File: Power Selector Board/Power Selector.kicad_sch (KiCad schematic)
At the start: 23 parts, among them J101 MSD-DB01M-12P, J102 MSD-DB01F-12P_1, J103 64900221122, J104 64900221122, J105 64900221122, K101 G6SK-2G DC24, K102 J115F11C24VDCSH.9, K103 J115F11C24VDCSH.9, U101 1720466, U102 LMW78_24-0.3RL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

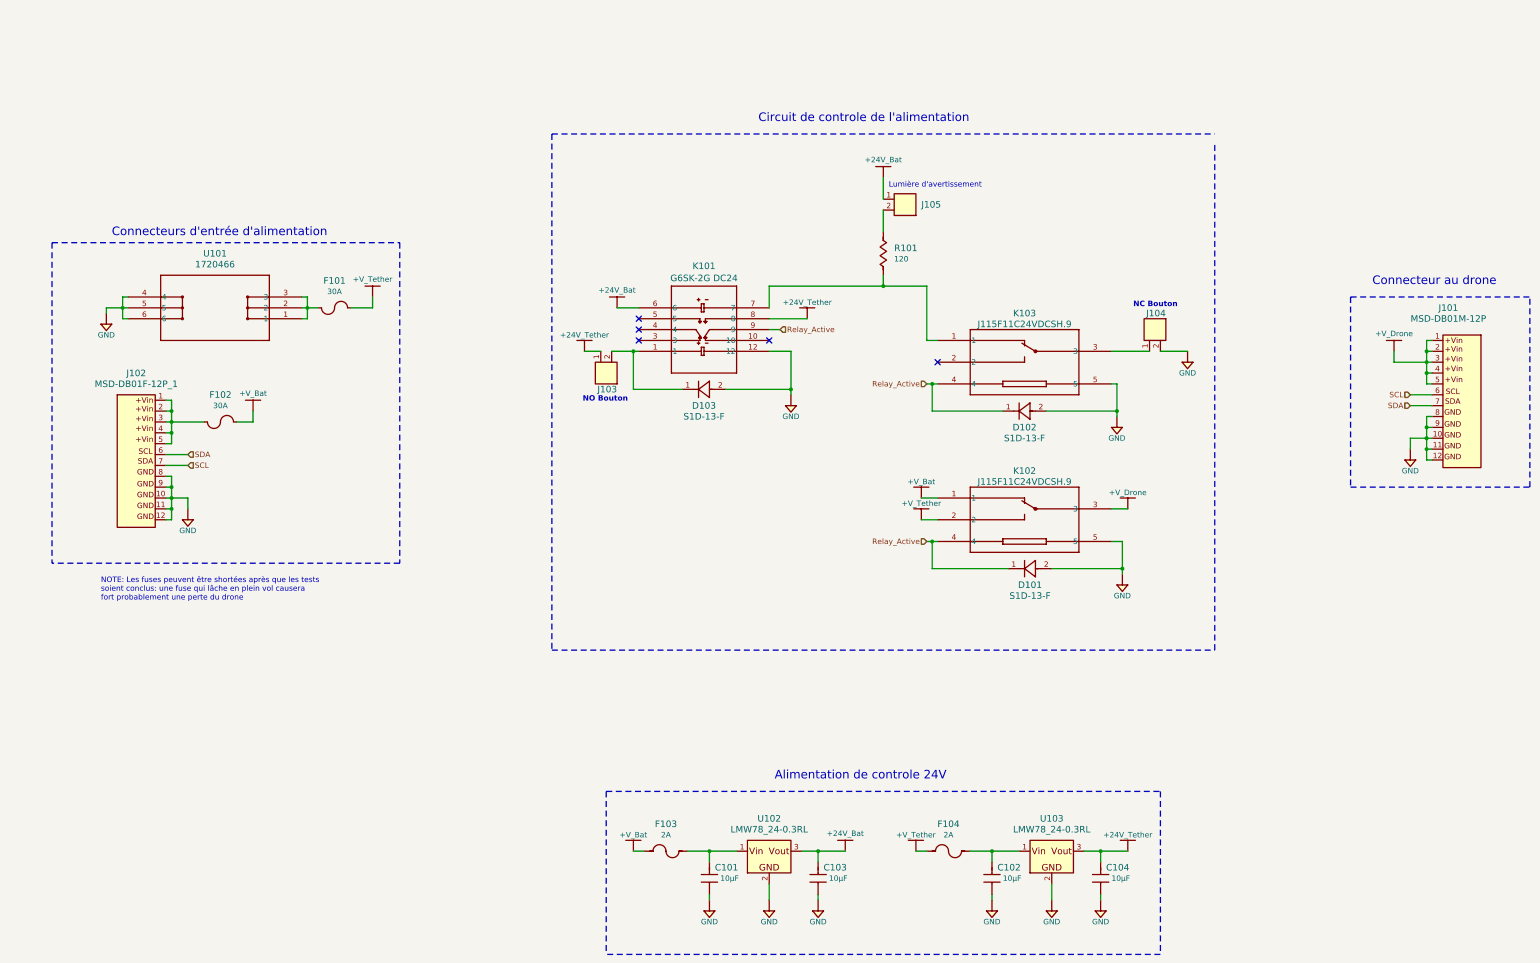
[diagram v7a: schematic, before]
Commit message: Ajout des deux PCB (droit et gauche) sur le meme PCB
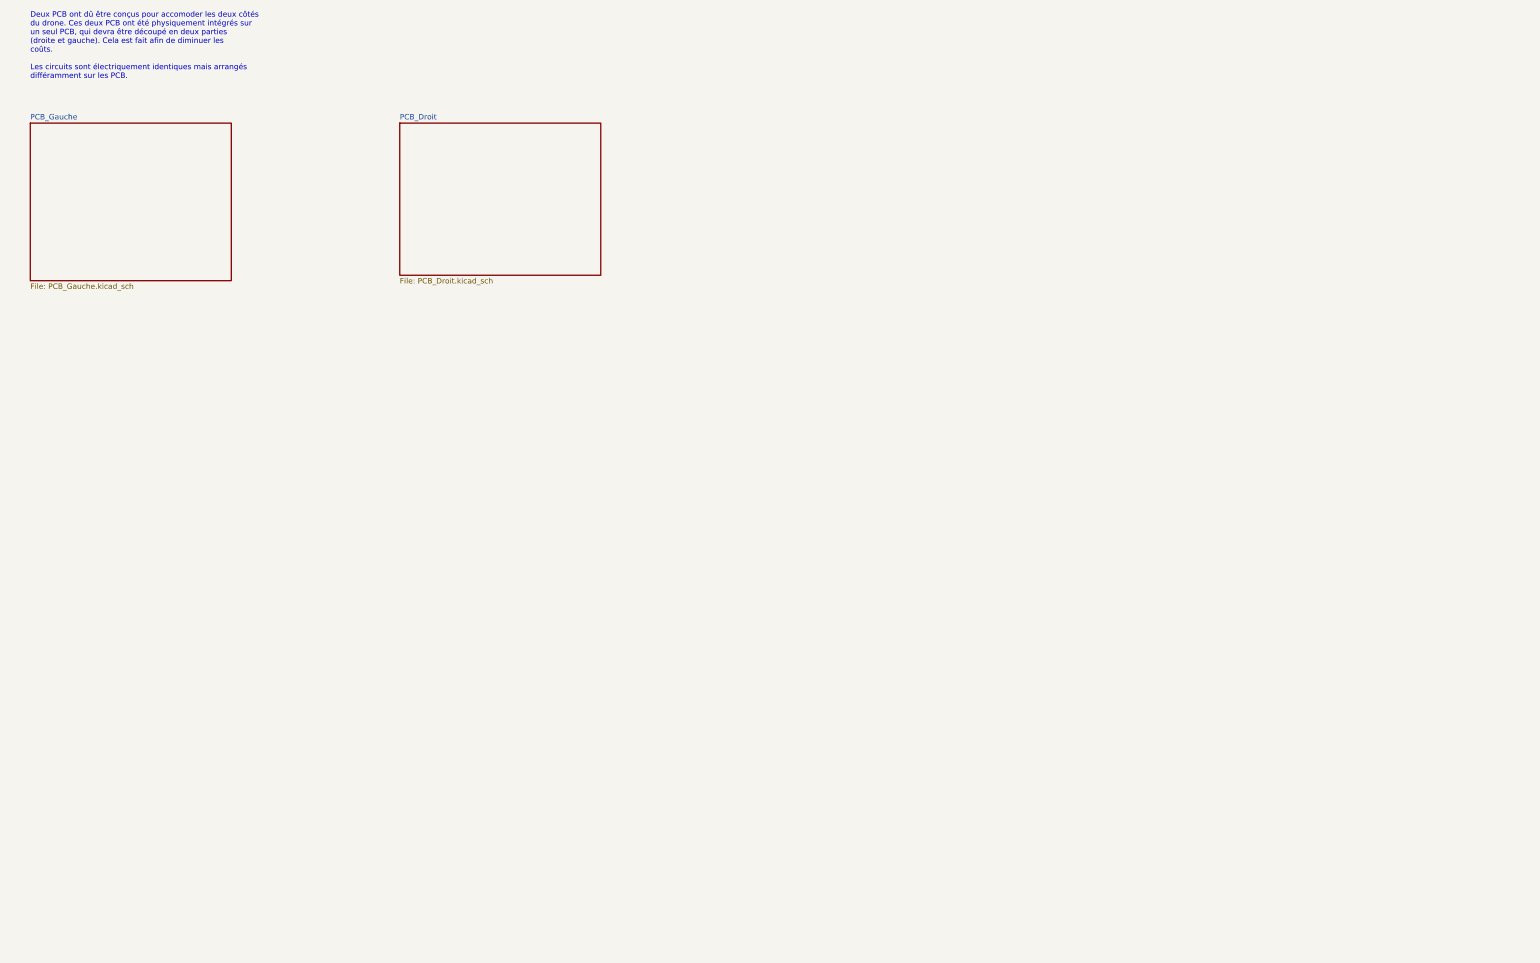
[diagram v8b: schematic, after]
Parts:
- removed C101, C102, C103, C104: GRM32EC72A106ME05L, Capacitors:C1210, symbol Capacitors:GRM32EC72A106ME05L
- removed D101, D102, D103: S1D-13-F, Diodes:SMA_DIO, symbol Diodes:S1D-13-F
- removed F101, F102: 047706.3MRET1P, Fuses:3587TR, symbol Fuses:047706.3MRET1P
- removed F103, F104: 0698Q2000-02, Fuses:TE5_395, symbol Fuses:0698Q2000-02
- removed J101: MSD-DB01M-12P, Connectors:649012227222, symbol Connectors:MSD-DB01M-12P
- removed J102: MSD-DB01F-12P_1, Connectors:649012227222, symbol Connectors:MSD-DB01F-12P_1
- removed J103, J104, J105: 64900221122, Connectors:64900221122, symbol Connectors:64900221122
- removed K101: G6SK-2G DC24, Relays:G6SK-2G DC3_OMR, symbol Relays:G6SK-2G_DC24
- removed K102, K103: J115F11C24VDCSH.9, RELAY5_J115F11C24VDCSH.9_CRS, symbol Relays:J115F11C24VDCSH.9
- removed R101: RC1206JR-07120RL, Resistors:R1206, symbol Resistors:RC1206JR-07120RL
- removed U101: 1720466, Connectors:1720466_PXC, symbol Connectors:1720466
- removed U102, U103: LMW78_24-0.3RL, Assembly:OKI-78SR_Horizontal, symbol PMIC:LMW78_24-0.3RL
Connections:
- no-connect marks 5 -> 0
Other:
- added sheet PCB_Droit (PCB_Droit.kicad_sch)
- added sheet PCB_Gauche (PCB_Gauche.kicad_sch)
- note added: "Deux PCB ont dû être conçus pour accomoder les deux côtés du drone. Ces deux PCB ont été physiquement intégrés sur un seul PCB, qui devra être découpé en deux parties (droite et gauche). Cela est fait afin de diminuer les coûts. Les circuits sont électriquement identiques mais arrangés différamment sur les PCB."
- note removed: "Alimentation de controle 24V"
- note removed: "Circuit de controle de l'alimentation"
- note removed: "Connecteur au drone"
- note removed: "Connecteurs d'entrée d'alimentation"
- note removed: "Lumière d'avertissement"
- note removed: "NC Bouton"
- note removed: "NO Bouton"
- note removed: "NOTE: Les fuses peuvent être shortées après que les tests soient conclus: une fuse qui lâche en plein vol causera fort probablement une perte du drone"
